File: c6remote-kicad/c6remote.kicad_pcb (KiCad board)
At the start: 2 copper layers, 37 x 130 mm, 50 parts, among them J1 Battery, Q1 MMBT2222A, Q2 AO3401A, SW1 SW_Push, SW10 SW_Push, SW11 SW_Push, SW2 SW_Push, SW3 SW_Push, SW4 SW_Push, SW5 SW_Push, SW6 SW_Push, SW7 SW_Push, SW8 SW_Push, SW9 SW_Push, U1 XIAO-ESP32-C6, U2 TSOP4136, U3 PCF8575DBR

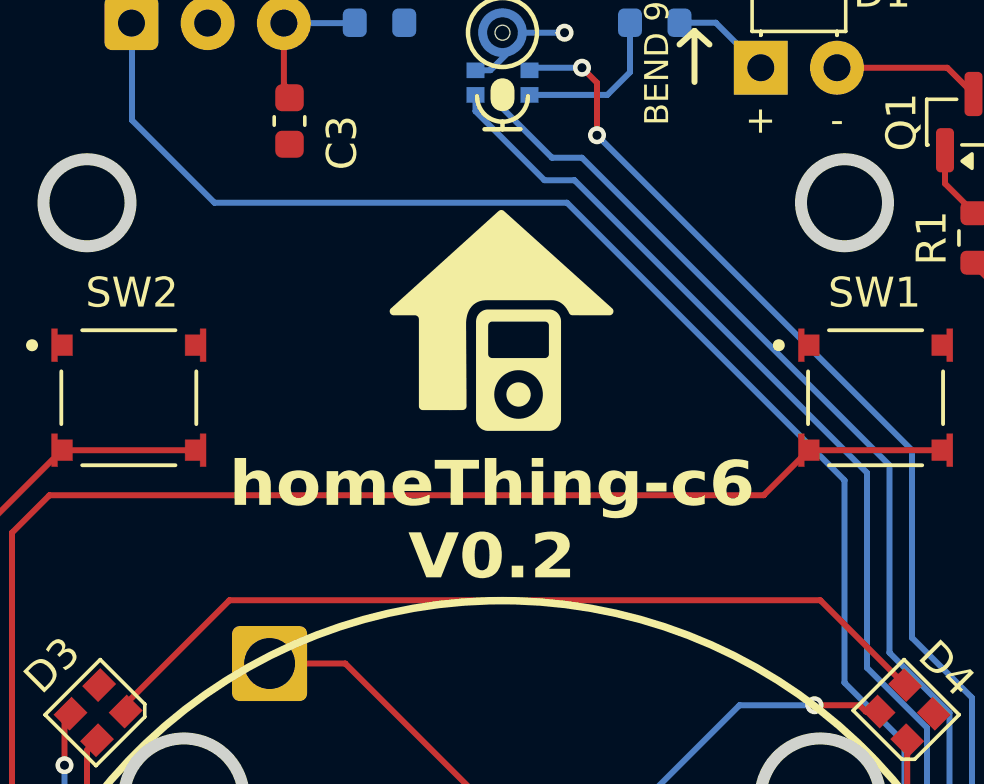
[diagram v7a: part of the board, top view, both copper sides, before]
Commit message: feat(pcb): renumber the board revision marking and the v0.1 release to ESPHome-style CalVer so the printed silk, the git tags and the GitHub releases all use one scheme; the front silk now carries homeThing-c6 at (53, 45.25) size 1.5 by 1.6 and a separate 2026.7.0 line at (53, 47.5) size 1 by 1 thickness 0.25, split into two gr_text items rather than one two-line block because the revision string went from 4 characters to 8 and wanted its own size, and 2026.7.0 at the smaller size clears SW2's courtyard by more than 4mm on the left, SW1's pin-1 dot by more than 4mm on the right, and leaves the gap to the ANO wheel outline at 50.514 unchanged; the v0.1 tag and release were renamed 2026.6.0, mapped from the 2026-06-16 fab date at 70ab9b0 rather than from the release-publication date, with the asset renamed c6remote-2026.6.0-fab.zip and a paragraph added to the release body recording the rename, that the old releases/tag/v0.1 and releases/download/v0.1 URLs are dead, and that the physical unit 1 board still reads V0.1 on its silk because it was fabbed under the old scheme and that marking cannot change; timeline, README and AGENTS.md follow the three links to the new tag, the Unit 1 heading takes the new number, and the tell-them-apart-in-a-photo line now reads V0.1 against 2026.7.0 with a note that the two differ in format rather than only in value; AGENTS.md reverses its own earlier claim that v0.1 was being left alone, and gains the rule that the silk revision must equal the release the board ships in, so a merge that slips into a later month needs the silk updated before merging rather than after, since the workflow computes the version from the merge date and not from the board; the ESPHome revision substitutions of v1, v2 and dev in the bring-up configs are deliberately untouched, they select which test firmware is flashed and are a separate namespace from the hardware version; silk only, no copper touched, zones still 2 F.Cu islands at 2316.3 and 735.9mm2 with t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
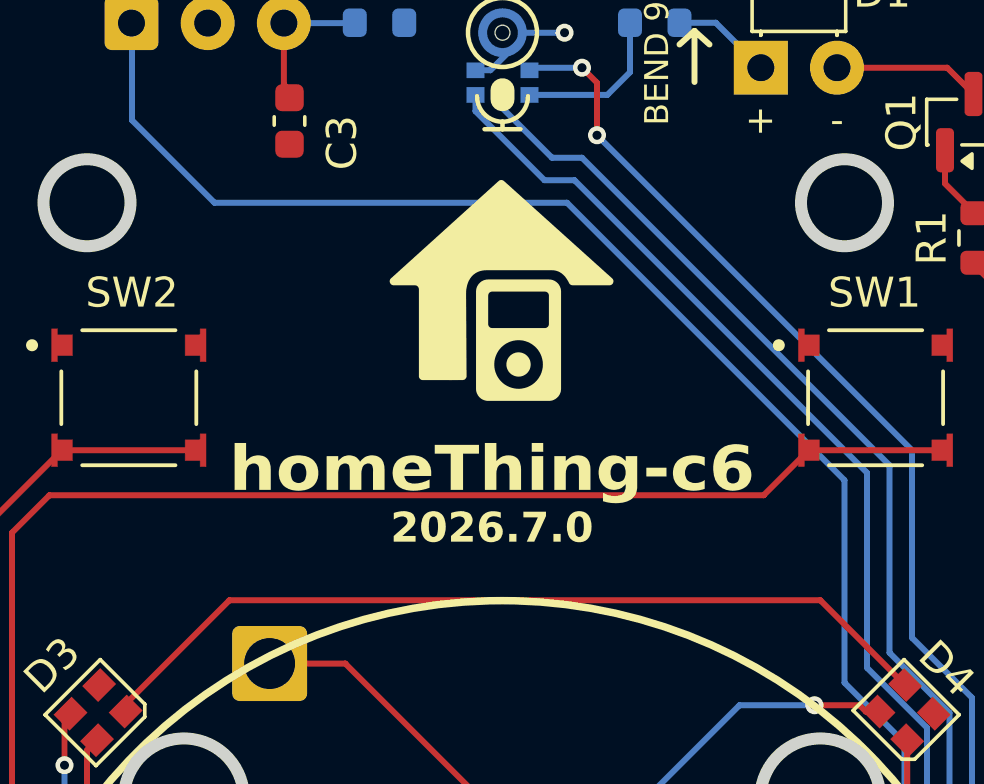
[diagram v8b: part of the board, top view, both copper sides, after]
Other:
- board text added: "2026.7.0"
- board text added: "homeThing-c6"
- board text removed: "homeThing-c6 V0.2"
